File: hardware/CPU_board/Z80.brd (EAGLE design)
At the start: 167.9 x 122.5 mm, 46 parts, among them IC11 74HCT245DW, IC3 ATF16V8BP3, IC6 74AC273N, IC9 74HCT138N

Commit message: CPU board update
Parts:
- removed C11: 100n, rcl:C0805
- removed C15, C21, C6: 100n, rcl:C1206
- added JP3: (no value), pinhead:1X02
- added R14: 10k, rcl:0204/7
- IC3: value ATF16V8BP3 -> (none); device atmel:DIL20 -> pal:DIL20
- R1, R8: device rcl:0207/12 -> rcl:0204/7
- R10: device rcl:0204/7 -> rcl:R0603
- R4: device rcl:R1206 -> rcl:R0603
- R9: device rcl:0204/7 -> rcl:0207/10
- moved C16 129.8 mm to (27.9, 112.9), turned to 90 degrees
- moved C22 43.6 mm to (25.9, 22.3), turned to 270 degrees
- moved C14 19.0 mm to (100.8, 15.9), turned to 0 degrees
- moved R10 16.9 mm to (19.7, 39.0), flipped to the bottom
- moved C10 11.1 mm to (134.0, 116.2), turned to 0 degrees
- moved R13 6.75 mm to (13.8, 14.9)
- moved C23 5.08 mm to (20.3, 8.57)
- moved LED1 4.58 mm to (9.84, 16.2), turned to 90 degrees
- moved IC3 4.44 mm to (116.2, 12.1)
- moved C13 4.26 mm to (144.5, 25.1)
- moved IC9 4.02 mm to (140.7, 13.3)
- moved R9 3.18 mm to (132.7, 19.1)
- moved R1 2.54 mm to (21.6, 19.4)
- moved R8 2.54 mm to (21.6, 15.6)
- moved R4 1.27 mm to (22.9, 88.3)
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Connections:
- removed net CF_DELAYED_RD: CON1.34
- removed net CF_DELAYED_WR: CON1.35
- removed net CS_1: IC9.14, SV2.58
- net !IORQ: now also IC3.8; no longer IC3.4
- net !MREQ: now also IC3.5; no longer IC3.1
- net !RESET: now also R14.1
- net A15: now also IC3.6; no longer IC3.3
- net A4: now also IC3.3; no longer IC3.7
- net CF_CS0: now also IC3.17
- net CLK: now also IC3.1
- net CS_EPROM: now also IC3.13; no longer IC3.17
- net DMA_CS: now also IC9.14; no longer IC3.14
- net GND: now also JP3.2, SV2.58; no longer C11.2, C15.2, C21.2, C6.2
- net INTA: now also IC3.12; no longer IC3.16
- net LOCAL_IO_CS: now also IC3.9; no longer IC3.6
- net M1: now also IC3.2; no longer IC3.5
- net RD: now also CON1.34
- net ROM_SHADOW: now also IC3.7; no longer IC3.2
- net VCC: now also JP3.1, R14.2; no longer C11.1, C15.1, C21.1, C6.1
- net WR: now also CON1.35, IC3.4
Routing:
- net VCC: track 540.5 -> 696.8 mm, vias 11 -> 14
- net RD: track 205.9 -> 344.6 mm, vias 4 -> 8
- net M1: track 99.9 -> 217.9 mm, vias 2 -> 4
- net D1: track 188.3 -> 287.7 mm
- net DMA_CS: track 70.8 -> 164.3 mm, vias 2 -> 4
- net WR: track 211.0 -> 286.6 mm, vias 6 -> 10
- net !IORQ: track 146.7 -> 209.2 mm, vias 6 -> 8
- net CF_CS0: track 48.0 -> 110.4 mm, vias 2 -> 4
- net A4: track 145.5 -> 201.9 mm, vias 0 -> 2
- net !MREQ: track 112.0 -> 163.7 mm, vias 2 -> 4
- net GND: track 108.3 -> 152.5 mm, vias 6 -> 14
- net CF_DELAYED_RD: track 42.4 -> 0.00 mm, vias 2 -> 0
- net CF_DELAYED_WR: track 41.2 -> 0.00 mm, vias 2 -> 0
- net CS_RAM1: track 58.9 -> 98.2 mm
- net CLK: track 210.5 -> 238.4 mm, vias 4 -> 6
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
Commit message: CPU board update
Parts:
- added C4: 100n, rcl:C0603
- added D1: 1N4148DO35-7, diode:DO35-7
- added JP1: (no value), pinhead:1X02
- added R15: (no value), rcl:R0603
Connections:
- new net N$2: JP1.2, R15.1
- net !RESET: now also C4.1, D1.A, R15.2
- net GND: now also C4.2, JP1.1
- net VCC: now also D1.C
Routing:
- net !RESET: track 271.1 -> 277.1 mm
- net N$2: track 0.00 -> 1.80 mm
- net CS_RAM1: track 98.2 -> 99.3 mm
- net VCC: track 696.8 -> 697.8 mm
- net D0: track 254.9 -> 254.2 mm
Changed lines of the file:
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@@
 <element name="JP3" library="pinhead" package="1X02" value="" x="9.2075" y="24.4475" rot="R180"/>
 <element name="R14" library="rcl" package="0204/7" value="10k" x="10.16" y="85.725" rot="R180"/>
+<element name="C4" library="rcl" package="C0603" value="100n" x="11.43" y="85.725" rot="MR0"/>
+<element name="D1" library="diode" package="DO35-7" value="1N4148DO35-7" x="9.2075" y="88.5825"/>
+<element name="R15" library="rcl" package="R0603" value="" x="13.55" y="91.1225" rot="MR270"/>
+<element name="JP1" library="pinhead" package="1X02" value="" x="10.4775" y="91.9725"/>
 </elements>
 <signals>
@@
 <wire x1="17.4625" y1="14.9225" x2="17.78" y2="14.605" width="0.6096" layer="16"/>
 <contactref element="R14" pad="2"/>
-<wire x1="6.35" y1="102.87" x2="6.35" y2="85.725" width="1.27" layer="16"/>
+<wire x1="6.35" y1="102.87" x2="6.35" y2="88.265" width="1.27" layer="16"/>
+<wire x1="6.35" y1="88.265" x2="6.35" y2="85.725" width="1.27" layer="16"/>
 <wire x1="6.35" y1="85.725" x2="6.35" y2="45.72" width="1.27" layer="16"/>
+<contactref element="D1" pad="C"/>
+<wire x1="5.3975" y1="88.5825" x2="6.0325" y2="88.5825" width="0.6096" layer="16"/>
+<wire x1="6.0325" y1="88.5825" x2="6.35" y2="88.265" width="0.6096" layer="16"/>
 <wire x1="10.4766" y1="24.4484" x2="10.4775" y2="24.4475" width="0" layer="19" extent="16-16"/>
 </signal>
@@
 <wire x1="46.99" y1="17.4625" x2="46.6725" y2="17.145" width="0.4064" layer="16"/>
 <wire x1="48.26" y1="17.4625" x2="48.5775" y2="17.145" width="0.4064" layer="16"/>
-<wire x1="48.26" y1="25.7175" x2="48.26" y2="21.32" width="0.4064" layer="16"/>
-<wire x1="48.26" y1="25.7175" x2="48.895" y2="26.3525" width="0.4064" layer="16"/>
+<wire x1="48.26" y1="25.4" x2="48.26" y2="21.32" width="0.4064" layer="16"/>
+<wire x1="48.26" y1="25.4" x2="48.895" y2="26.035" width="0.4064" layer="16"/>
 <contactref element="C7" pad="2"/>
 <contactref element="IC11" pad="10"/>
@@
 <contactref element="SV2" pad="58"/>
 <contactref element="JP3" pad="2"/>
+<contactref element="C4" pad="2"/>
+<contactref element="JP1" pad="1"/>
 </signal>
 <signal name="D0">
@@
 <wire x1="32.7025" y1="83.185" x2="25.4" y2="83.185" width="0.4064" layer="16"/>
 <wire x1="25.4" y1="83.185" x2="24.13" y2="84.455" width="0.4064" layer="16"/>
-<wire x1="24.13" y1="84.455" x2="12.7" y2="84.455" width="0.4064" layer="16"/>
-<via x="12.7" y="84.455" extent="1-16" drill="0.6" diameter="1.4224" shape="octagon"/>
-<wire x1="12.7" y1="84.455" x2="12.7" y2="33.02" width="0.4064" layer="1"/>
+<via x="12.7" y="83.185" extent="1-16" drill="0.6" diameter="1.4224" shape="octagon"/>
+<wire x1="12.7" y1="83.185" x2="12.7" y2="33.02" width="0.4064" layer="1"/>
 <via x="12.7" y="33.02" extent="1-16" drill="0.6" diameter="1.4224" shape="octagon"/>
 <wire x1="12.7" y1="33.02" x2="15.24" y2="33.02" width="0.4064" layer="16"/>
 <wire x1="15.24" y1="33.02" x2="19.685" y2="28.575" width="0.4064" layer="16"/>
 <wire x1="19.685" y1="28.575" x2="22.9108" y2="28.575" width="0.4064" layer="16"/>
+<wire x1="24.13" y1="84.455" x2="15.875" y2="84.455" width="0.4064" layer="16"/>
+<wire x1="15.875" y1="84.455" x2="14.605" y2="83.185" width="0.4064" layer="16"/>
+<wire x1="14.605" y1="83.185" x2="12.7" y2="83.185" width="0.4064" layer="16"/>
 </signal>
 <signal name="D1">
@@
 <wire x1="30.1625" y1="75.565" x2="17.4625" y2="75.565" width="0.4064" layer="16"/>
 <contactref element="CON1" pad="20"/>
-<wire x1="43.18" y1="21.32" x2="43.18" y2="27.305" width="0.4064" layer="16"/>
-<via x="44.1325" y="28.2575" extent="1-16" drill="0.6" diameter="1.4224" shape="octagon"/>
+<wire x1="43.18" y1="21.32" x2="43.18" y2="28.2575" width="0.4064" layer="16"/>
+<via x="44.1325" y="29.21" extent="1-16" drill="0.6" diameter="1.4224" shape="octagon"/>
 <via x="44.1325" y="76.835" extent="1-16" drill="0.6" diameter="1.4224" shape="octagon"/>
-<wire x1="44.1325" y1="28.2575" x2="44.1325" y2="76.835" width="0.4064" layer="1"/>
+<wire x1="44.1325" y1="29.21" x2="44.1325" y2="76.835" width="0.4064" layer="1"/>
 <wire x1="31.4325" y1="76.835" x2="44.1325" y2="76.835" width="0.4064" layer="16"/>
 <wire x1="44.1325" y1="76.835" x2="50.4825" y2="76.835" width="0.4064" layer="16"/>
-<wire x1="43.18" y1="27.305" x2="44.1325" y2="28.2575" width="0.4064" layer="16"/>
+<wire x1="43.18" y1="28.2575" x2="44.1325" y2="29.21" width="0.4064" layer="16"/>
 </signal>
 <signal name="A1">
@@
 <contactref element="IC11" pad="1"/>
 <wire x1="28.8925" y1="84.455" x2="26.9875" y2="86.36" width="0.4064" layer="16"/>
-<wire x1="26.9875" y1="86.36" x2="24.4475" y2="86.36" width="0.4064" layer="16"/>
-<wire x1="24.4475" y1="86.36" x2="23.8125" y2="86.995" width="0.4064" layer="16"/>
-<wire x1="23.8125" y1="86.995" x2="15.24" y2="86.995" width="0.4064" layer="16"/>
+<wire x1="26.9875" y1="86.36" x2="22.5425" y2="86.36" width="0.4064" layer="16"/>
+<wire x1="22.5425" y1="86.36" x2="21.9075" y2="86.995" width="0.4064" layer="16"/>
+<wire x1="21.9075" y1="86.995" x2="15.24" y2="86.995" width="0.4064" layer="16"/>
 <via x="15.24" y="86.995" extent="1-16" drill="0.6" diameter="1.4224" shape="octagon"/>
 <wire x1="15.24" y1="86.995" x2="15.24" y2="29.845" width="0.4064" layer="1"/>
@@
 <wire x1="107.315" y1="93.98" x2="107.315" y2="42.545" width="0.4064" layer="1"/>
 <contactref element="CON1" pad="41"/>
-<via x="50.4825" y="28.2575" extent="1-16" drill="0.6" diameter="1.4224" shape="octagon"/>
-<wire x1="50.4825" y1="46.6725" x2="50.4825" y2="28.2575" width="0.4064" layer="1"/>
-<wire x1="47.625" y1="21.32" x2="47.625" y2="26.3525" width="0.4064" layer="16"/>
+<via x="49.8475" y="28.2575" extent="1-16" drill="0.6" diameter="1.4224" shape="octagon"/>
+<wire x1="49.8475" y1="46.6725" x2="49.8475" y2="28.2575" width="0.4064" layer="1"/>
+<wire x1="47.625" y1="21.32" x2="47.625" y2="26.035" width="0.4064" layer="16"/>
 <wire x1="65.0875" y1="46.6725" x2="67.945" y2="43.815" width="0.4064" layer="16"/>
 <wire x1="20.955" y1="48.26" x2="33.02" y2="48.26" width="0.4064" layer="16"/>
 <wire x1="33.02" y1="48.26" x2="34.6075" y2="46.6725" width="0.4064" layer="16"/>
 <wire x1="138.7475" y1="42.545" x2="107.315" y2="42.545" width="0.4064" layer="16"/>
-<via x="50.4825" y="46.6725" extent="1-16" drill="0.6" diameter="1.4224" shape="octagon"/>
-<wire x1="34.6075" y1="46.6725" x2="50.4825" y2="46.6725" width="0.4064" layer="16"/>
-<wire x1="50.4825" y1="46.6725" x2="65.0875" y2="46.6725" width="0.4064" layer="16"/>
+<via x="49.8475" y="46.6725" extent="1-16" drill="0.6" diameter="1.4224" shape="octagon"/>
+<wire x1="34.6075" y1="46.6725" x2="49.8475" y2="46.6725" width="0.4064" layer="16"/>
+<wire x1="49.8475" y1="46.6725" x2="65.0875" y2="46.6725" width="0.4064" layer="16"/>
 <wire x1="17.4625" y1="85.725" x2="20.955" y2="85.725" width="0.635" layer="16"/>
-<wire x1="50.4825" y1="28.2575" x2="49.53" y2="28.2575" width="0.4064" layer="16"/>
-<wire x1="49.53" y1="28.2575" x2="47.625" y2="26.3525" width="0.4064" layer="16"/>
-<contactref element="R14" pad="1"/>
-<wire x1="13.97" y1="85.725" x2="17.4625" y2="85.725" width="0.6096" layer="16"/>
 <wire x1="107.315" y1="42.545" x2="93.345" y2="42.545" width="0.4064" layer="16"/>
 <wire x1="93.345" y1="42.545" x2="92.075" y2="43.815" width="0.4064" layer="16"/>
 <wire x1="92.075" y1="43.815" x2="67.945" y2="43.815" width="0.4064" layer="16"/>
+<contactref element="R14" pad="1"/>
+<wire x1="13.97" y1="85.725" x2="17.4625" y2="85.725" width="0.4064" layer="16"/>
+<contactref element="C4" pad="1"/>
+<wire x1="12.28" y1="85.725" x2="13.335" y2="85.725" width="0.6096" layer="16"/>
+<contactref element="D1" pad="A"/>
+<wire x1="13.335" y1="85.725" x2="13.97" y2="85.725" width="0.6096" layer="16"/>
+<contactref element="R15" pad="2"/>
+<wire x1="13.0175" y1="88.5825" x2="13.55" y2="88.5825" width="0.6096" layer="16"/>
+<wire x1="13.55" y1="88.5825" x2="13.55" y2="90.2725" width="0.6096" layer="16"/>
+<wire x1="13.55" y1="88.5825" x2="13.55" y2="85.94" width="0.6096" layer="16"/>
+<wire x1="13.55" y1="85.94" x2="13.335" y2="85.725" width="0.6096" layer="16"/>
+<wire x1="47.625" y1="26.035" x2="49.8475" y2="28.2575" width="0.4064" layer="16"/>
 </signal>
 <signal name="SET_BANK_A14">
@@
 <signal name="CS_RAM1">
 <contactref element="U$4" pad="20"/>
-<via x="88.9" y="13.335" extent="1-16" drill="0.6" diameter="1.4224" shape="octagon"/>
-<wire x1="88.9" y1="13.335" x2="88.9" y2="70.485" width="0.4064" layer="1"/>
+<via x="88.9" y="17.78" extent="1-16" drill="0.6" diameter="1.4224" shape="octagon"/>
+<wire x1="88.9" y1="17.78" x2="88.9" y2="70.485" width="0.4064" layer="1"/>
 <via x="88.9" y="70.485" extent="1-16" drill="0.6" diameter="1.4224" shape="octagon"/>
 <wire x1="88.9" y1="70.485" x2="80.645" y2="70.485" width="0.4064" layer="16"/>
 <wire x1="80.645" y1="70.485" x2="79.375" y2="71.755" width="0.4064" layer="16"/>
 <wire x1="79.375" y1="71.755" x2="78.105" y2="71.755" width="0.4064" layer="16"/>
-<wire x1="95.885" y1="6.35" x2="88.9" y2="13.335" width="0.4064" layer="16"/>
 <contactref element="IC3" pad="19"/>
-<wire x1="95.885" y1="6.35" x2="105.41" y2="6.35" width="0.4064" layer="16"/>
+<wire x1="93.98" y1="6.35" x2="105.41" y2="6.35" width="0.4064" layer="16"/>
 <wire x1="105.41" y1="6.35" x2="106.045" y2="6.985" width="0.4064" layer="16"/>
 <wire x1="106.045" y1="6.985" x2="106.045" y2="9.525" width="0.4064" layer="16"/>
 <wire x1="106.045" y1="9.525" x2="107.315" y2="10.795" width="0.4064" layer="16"/>
 <wire x1="107.315" y1="10.795" x2="107.315" y2="15.875" width="0.4064" layer="16"/>
+<wire x1="88.9" y1="17.78" x2="88.9" y2="11.43" width="0.4064" layer="16"/>
+<wire x1="88.9" y1="11.43" x2="93.98" y2="6.35" width="0.4064" layer="16"/>
 </signal>
 <signal name="CS_RAM2">
@@
 <wire x1="9.8425" y1="17.4625" x2="15.24" y2="17.4625" width="0.8128" layer="16"/>
 </signal>
+<signal name="N$2">
+<contactref element="R15" pad="1"/>
+<contactref element="JP1" pad="2"/>
+<wire x1="11.7475" y1="91.9725" x2="13.55" y2="91.9725" width="0.6096" layer="16"/>
+</signal>
 </signals>

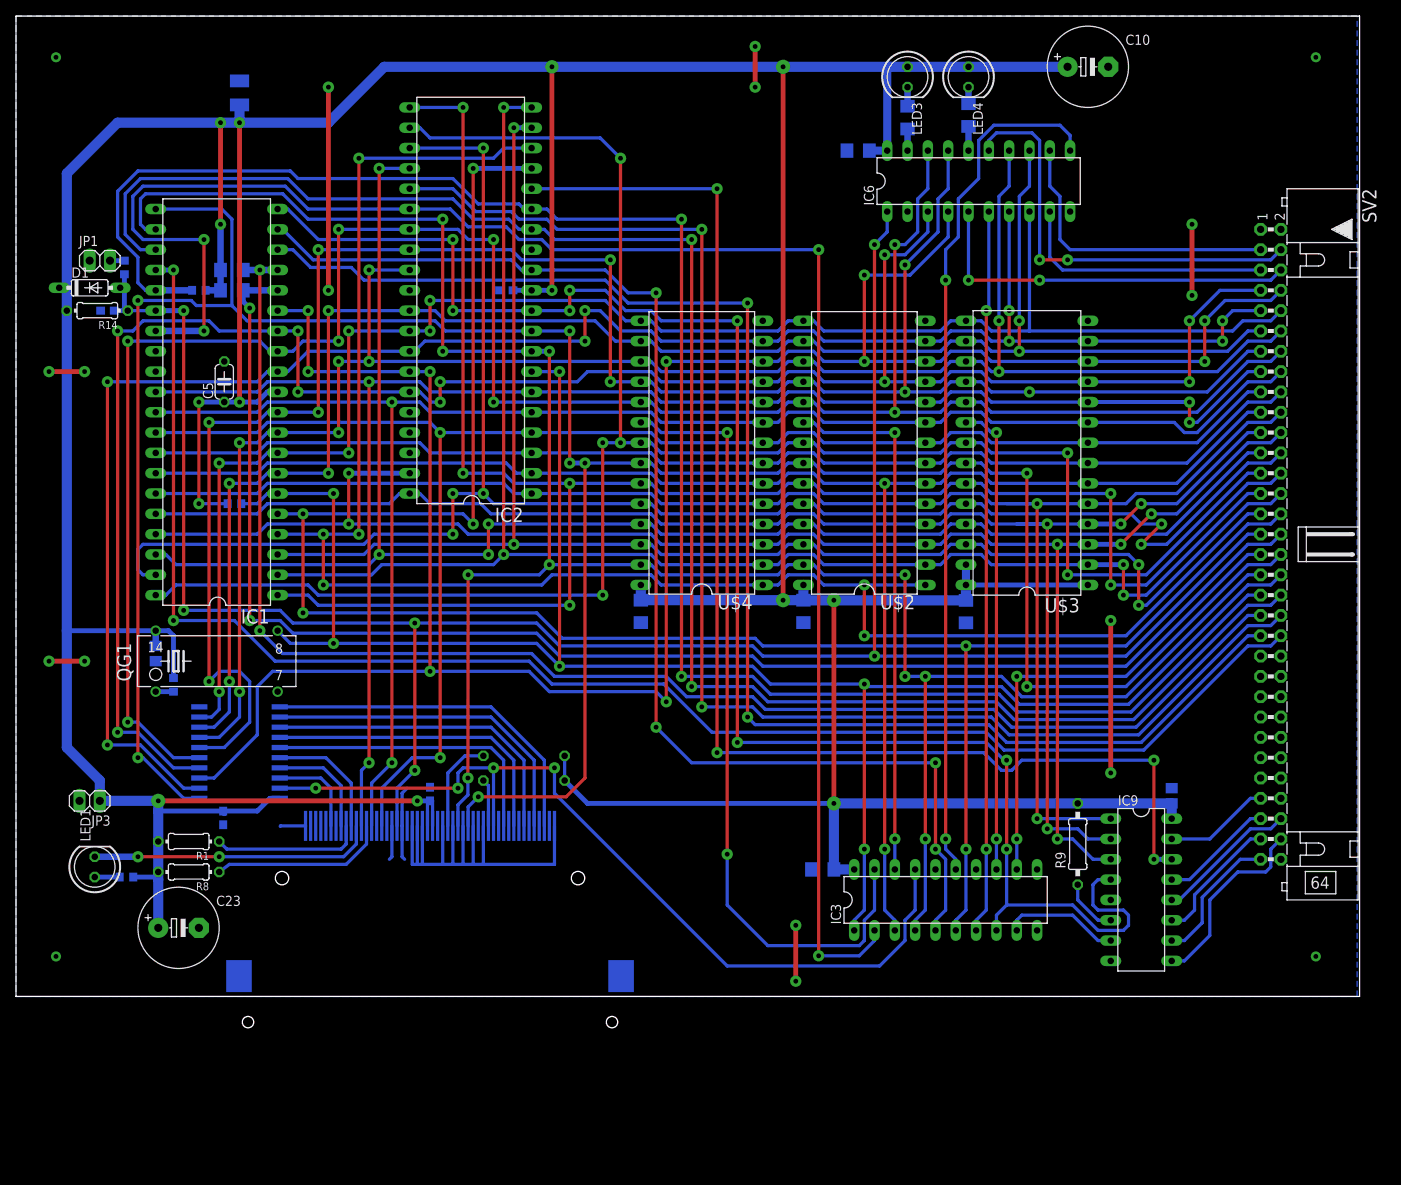
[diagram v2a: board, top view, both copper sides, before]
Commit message: bugs in CPU board design fixed
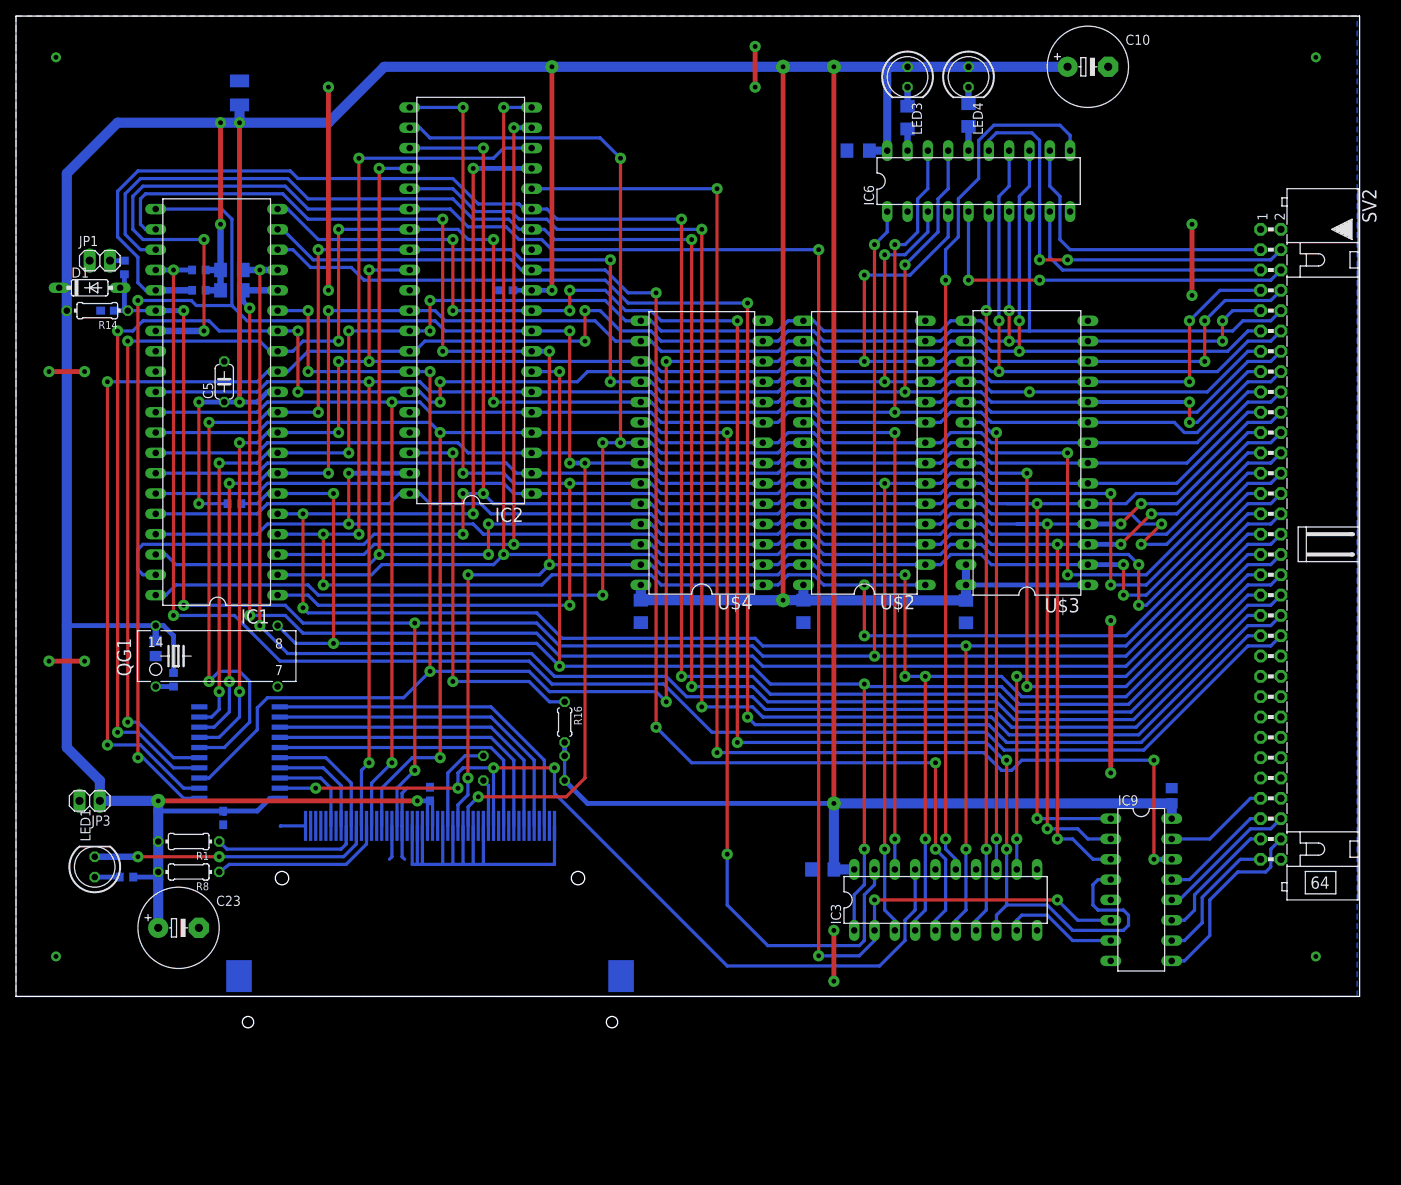
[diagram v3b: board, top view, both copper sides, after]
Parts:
- removed R9: 10k, rcl:0207/10
- added R16: (no value), rcl:0204/5
- added R17: (no value), rcl:R0603
- moved C12 0.64 mm to (17.5, 43.5)
- moved QG1 0.64 mm to (25.1, 42.5)
- moved R10 0.64 mm to (19.7, 39.6)
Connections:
- removed net N$20: IC9.6, R9.1
- new net N$3: IC2.38, R16.1
- net M1: now also IC9.6
- net VCC: now also R16.2, R17.2; no longer R9.2
- net WAIT: now also R17.1
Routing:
- net VCC: track 697.8 -> 767.6 mm
- net N$3: track 0.00 -> 49.0 mm, vias 0 -> 2
- net M1: track 217.9 -> 252.2 mm, vias 4 -> 6
- net N$20: track 7.08 -> 0.00 mm
- net A15: track 256.0 -> 253.8 mm
- net WAIT: track 197.1 -> 199.0 mm
- net D1: track 287.7 -> 285.8 mm
- net GND: track 152.2 -> 151.5 mm
